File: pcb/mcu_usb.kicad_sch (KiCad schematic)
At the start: 33 parts, among them J12 USB_C_Receptacle, J13 UPDI, U10 CP2102N-A02-GQFN24, U11 LP2985-3.3, U9 AVR128DA32-I/PT, Y1 32.768kHz

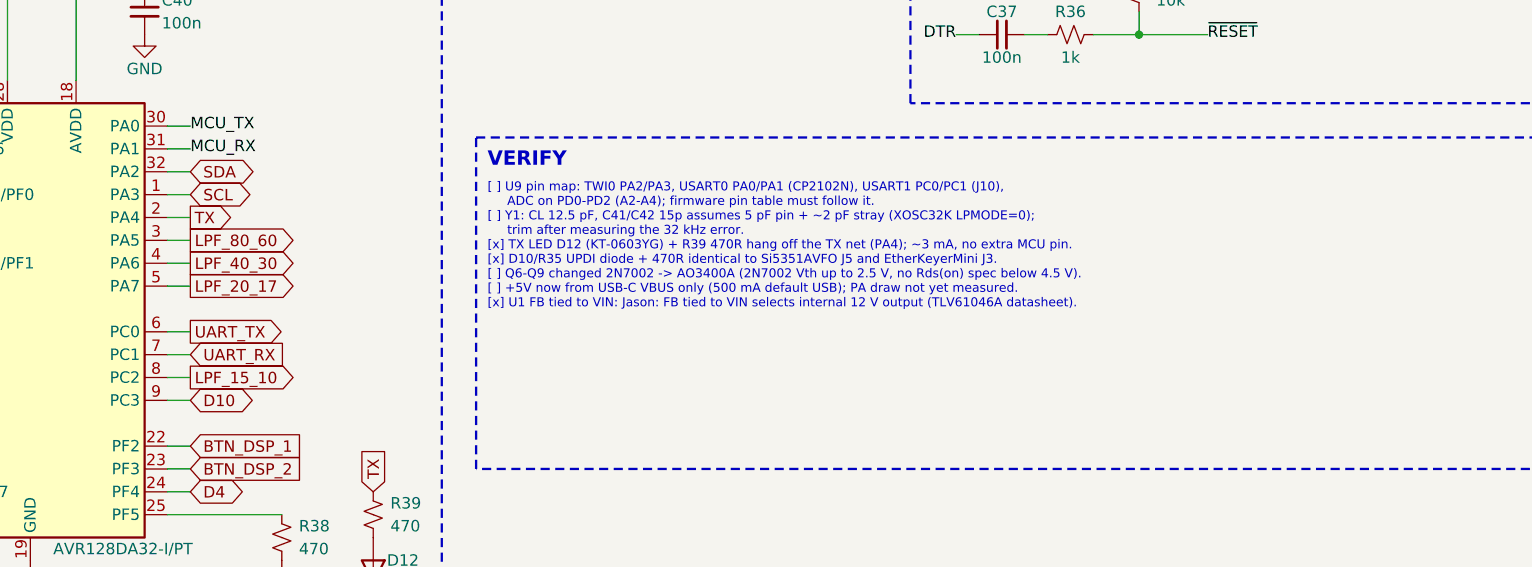
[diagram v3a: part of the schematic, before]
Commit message: Filter bank: 6-relay two-level tree driven by BAND_A/BAND_B
Replace the 8-relay, 4-driver bank with a 2-bit tree (K1-K3 input,
K4-K6 output, one G6K pole each). All relays off selects 80/60 m.
Q6/Q7 AO3400A drive the first and second levels; PA7/PC2 freed.
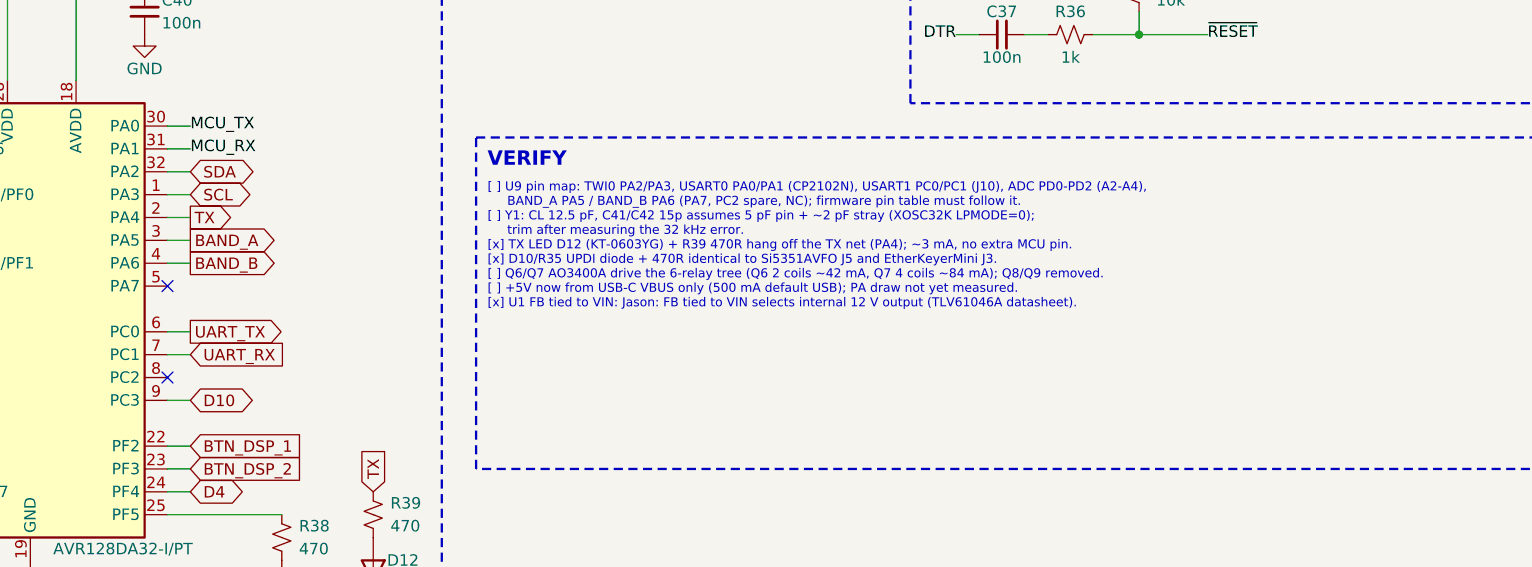
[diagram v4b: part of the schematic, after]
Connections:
- net LPF_15_10: no longer names the net of U9.8 (PC2)
- net LPF_20_17: no longer names the net of U9.5 (PA7)
- net LPF_40_30 renamed BAND_B
- net LPF_80_60 renamed BAND_A
- no-connect marks 15 -> 17
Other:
- note added: "[ ] U9 pin map: TWI0 PA2/PA3, USART0 PA0/PA1 (CP2102N), USART1 PC0/PC1 (J10), ADC PD0-PD2 (A2-A4), BAND_A PA5 / BAND_B PA6 (PA7, PC2 spare, NC); firmware pin table must follow it. [ ] Y1: CL 12.5 pF, C41/C42 15p assumes 5 pF pin + ~2 pF stray (XOSC32K LPMODE=0); trim after measuring the 32 kHz error. [x] TX LED D12 (KT-0603YG) + R39 470R hang off the TX net (PA4); ~3 mA, no extra MCU pin. [x] D10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"
- note removed: "[ ] U9 pin map: TWI0 PA2/PA3, USART0 PA0/PA1 (CP2102N), USART1 PC0/PC1 (J10), ADC on PD0-PD2 (A2-A4); firmware pin table must follow it. [ ] Y1: CL 12.5 pF, C41/C42 15p assumes 5 pF pin + ~2 pF stray (XOSC32K LPMODE=0); trim after measuring the 32 kHz error. [x] TX LED D12 (KT-0603YG) + R39 470R hang off the TX net (PA4); ~3 mA, no extra MCU pin. [x] D10/R35 UPDI diode + 470R identical to Si5351A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"
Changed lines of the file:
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@@
 		)
 	)
-	(global_label "LPF_80_60"
+	(global_label "BAND_A"
 		(shape output)
 		(at 119.38 139.7 0)
@@
 		)
 	)
-	(global_label "LPF_40_30"
+	(global_label "BAND_B"
 		(shape output)
 		(at 119.38 142.24 0)
@@
 		(property "Intersheetrefs" "${INTERSHEET_REFS}"
 			(at 119.38 142.24 0)
-			(effects
-				(font
-					(size 1.27 1.27)
-				)
-				(hide yes)
-			)
-		)
-	)
-	(wire
-		(pts
-			(xy 116.84 144.78)
-			(xy 119.38 144.78)
-		)
-		(stroke
-			(width 0)
-			(type default)
-		)
-	)
-	(global_label "LPF_20_17"
-		(shape output)
-		(at 119.38 144.78 0)
-		(fields_autoplaced yes)
-		(effects
-			(font
-				(size 1.27 1.27)
-				(color 0 120 120 1)
-			)
-			(justify left)
-		)
-		(property "Intersheetrefs" "${INTERSHEET_REFS}"
-			(at 119.38 144.78 0)
-			(effects
-				(font
-					(size 1.27 1.27)
-				)
-				(hide yes)
-			)
-		)
-	)
-	(wire
-		(pts
-			(xy 116.84 154.94)
-			(xy 119.38 154.94)
-		)
-		(stroke
-			(width 0)
-			(type default)
-		)
-	)
-	(global_label "LPF_15_10"
-		(shape output)
-		(at 119.38 154.94 0)
-		(fields_autoplaced yes)
-		(effects
-			(font
-				(size 1.27 1.27)
-				(color 0 120 120 1)
-			)
-			(justify left)
-		)
-		(property "Intersheetrefs" "${INTERSHEET_REFS}"
-			(at 119.38 154.94 0)
 			(effects
 				(font
@@
 			)
 		)
+	)
+	(no_connect
+		(at 116.84 144.78)
+	)
+	(no_connect
+		(at 116.84 154.94)
 	)
 	(wire
@@
 		)
 	)
-	(text "[ ] U9 pin map: TWI0 PA2/PA3, USART0 PA0/PA1 (CP2102N), USART1 PC0/PC1 (J10),\n     ADC on PD0-PD2 (A2-A4); firmware pin table must follow it.\n[ ] Y1: CL 12.5 pF, C41/C42 15p assumes 5 pF pin + ~2 pF stray (XOSC32K LPMODE=0);\n     trim after measuring the 32 kHz error.\n[x] TX LED D12 (KT-0603YG) + R39 470R hang off the TX net (PA4); ~3 mA, no extra MCU pin.\n[x] D10/R35 UPDI diode + 470R identical to Si5351AVFO J5 and EtherKeyerMini J3.\n[ ] Q6-Q9 changed 2N7002 -> AO3400A (2N7002 Vth up to 2.5 V, no Rds(on) spec below 4.5 V).\n[ ] +5V now from USB-C VBUS only (500 mA default USB); PA draw not yet measured.\n[x] U1 FB tied to VIN: Jason: FB tied to VIN selects internal 12 V output (TLV61046A datasheet)."
+	(text "[ ] U9 pin map: TWI0 PA2/PA3, USART0 PA0/PA1 (CP2102N), USART1 PC0/PC1 (J10), ADC PD0-PD2 (A2-A4),\n     BAND_A PA5 / BAND_B PA6 (PA7, PC2 spare, NC); firmware pin table must follow it.\n[ ] Y1: CL 12.5 pF, C41/C42 15p assumes 5 pF pin + ~2 pF stray (XOSC32K LPMODE=0);\n     trim after measuring the 32 kHz error.\n[x] TX LED D12 (KT-0603YG) + R39 470R hang off the TX net (PA4); ~3 mA, no extra MCU pin.\n[x] D10/R35 UPDI diode + 470R identical to Si5351AVFO J5 and EtherKeyerMini J3.\n[ ] Q6/Q7 AO3400A drive the 6-relay tree (Q6 2 coils ~42 mA, Q7 4 coils ~84 mA); Q8/Q9 removed.\n[ ] +5V now from USB-C VBUS only (500 mA default USB); PA draw not yet measured.\n[x] U1 FB tied to VIN: Jason: FB tied to VIN selects internal 12 V output (TLV61046A datasheet)."
 		(exclude_from_sim no)
 		(at 152.4 133.35 0)

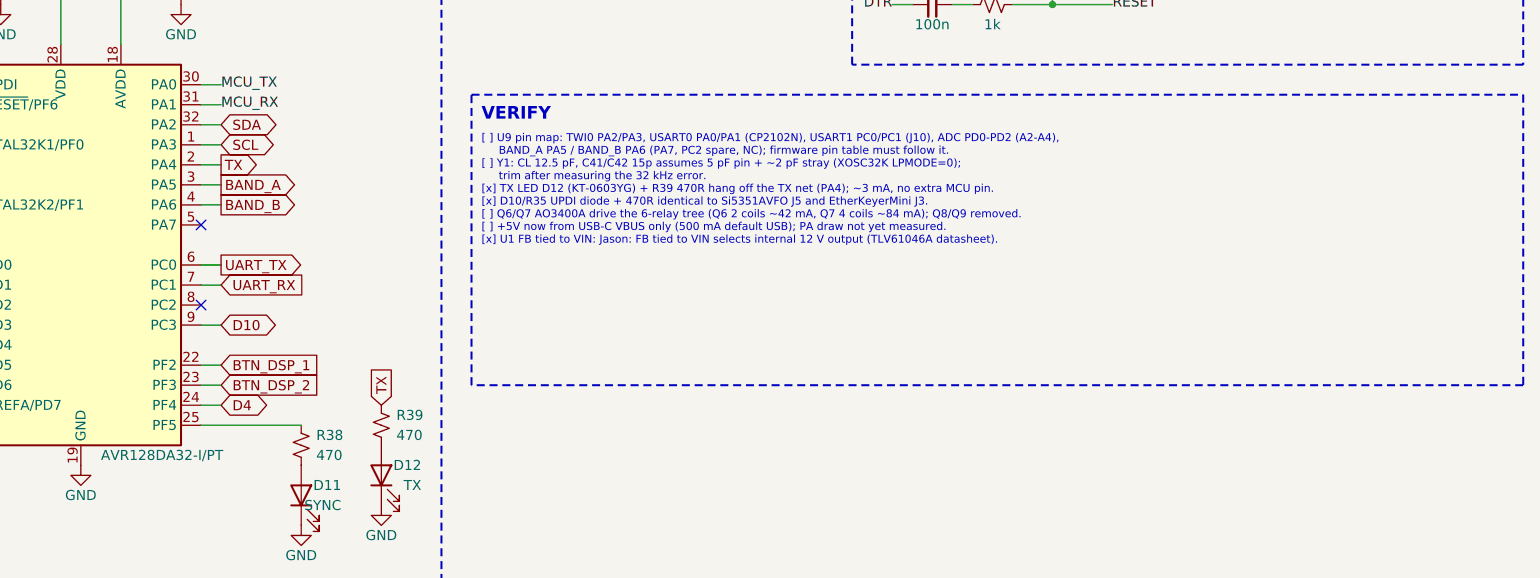
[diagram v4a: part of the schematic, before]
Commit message: Add GPS option sheet (u-blox MAX-M10S) on USART2 ALT1
- New pcb/gps.kicad_sch: MAX-M10S U12 on +3.3V (VIO_SEL open), UART to
  PF4/PF5, TIMEPULSE via 470R to GPS_PPS / J14, active-antenna bias-T
  (10R, 10n, 27nH per IM 4.3.4) to U.FL J15, supercap V_BCKP via
  1N5711W + 1k.
- MCU: D4 moved PF4 -> PA7, sync LED moved PF5 -> PC2.
- GPS_PPS MCU pin left open; options in VERIFY.md.
- Regenerated schematic PDF; ERC 0 errors.
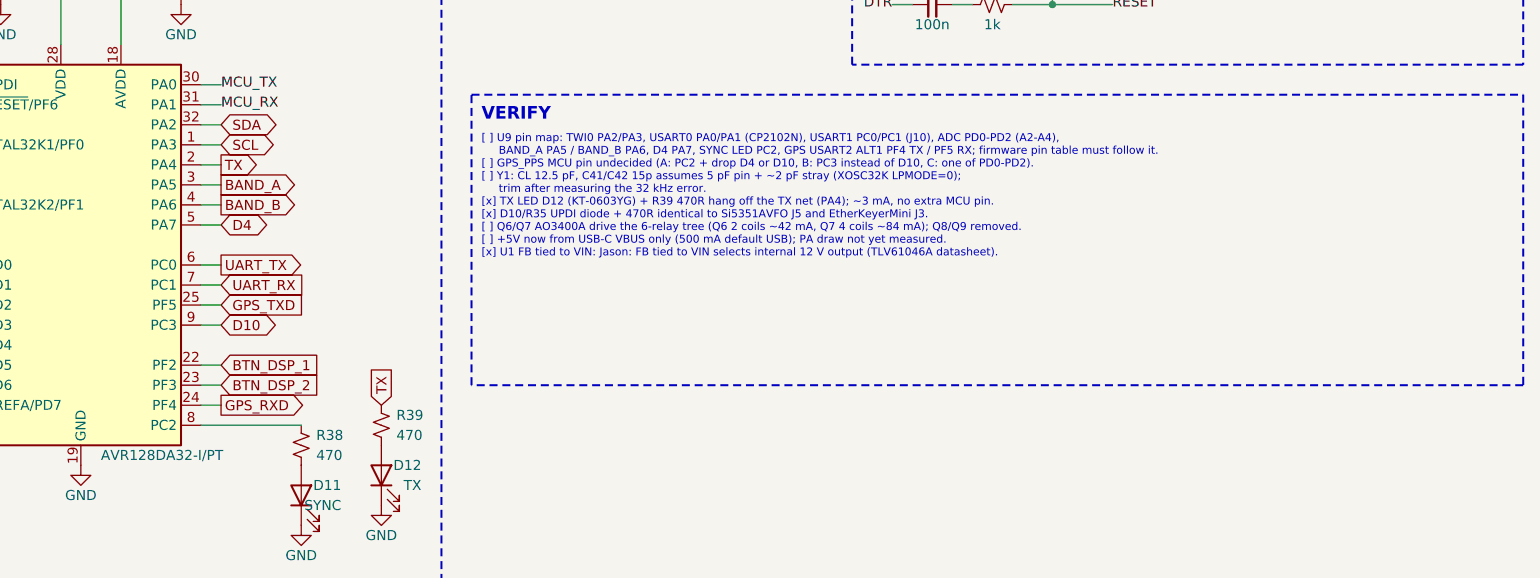
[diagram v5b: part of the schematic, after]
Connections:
- net D4: now also U9.5 (PA7); no longer U9.24 (PF4)
- net at R38.1: now also U9.8 (PC2); no longer U9.25 (PF5)
- new net GPS_RXD: U9.24 (PF4)
- new net GPS_TXD: U9.25 (PF5)
- no-connect marks 17 -> 15
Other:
- note added: "[ ] U9 pin map: TWI0 PA2/PA3, USART0 PA0/PA1 (CP2102N), USART1 PC0/PC1 (J10), ADC PD0-PD2 (A2-A4), BAND_A PA5 / BAND_B PA6, D4 PA7, SYNC LED PC2, GPS USART2 ALT1 PF4 TX / PF5 RX; firmware pin table must follow it. [ ] GPS_PPS MCU pin undecided (A: PC2 + drop D4 or D10, B: PC3 instead of D10, C: one of PD0-PD2). [ ] Y1: CL 12.5 pF, C41/C42 15p assumes 5 pF pin + ~2 pF stray (XOSC32K LPMODE=0); tri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"
- note removed: "[ ] U9 pin map: TWI0 PA2/PA3, USART0 PA0/PA1 (CP2102N), USART1 PC0/PC1 (J10), ADC PD0-PD2 (A2-A4), BAND_A PA5 / BAND_B PA6 (PA7, PC2 spare, NC); firmware pin table must follow it. [ ] Y1: CL 12.5 pF, C41/C42 15p assumes 5 pF pin + ~2 pF stray (XOSC32K LPMODE=0); trim after measuring the 32 kHz error. [x] TX LED D12 (KT-0603YG) + R39 470R hang off the TX net (PA4); ~3 mA, no extra MCU pin. [x] D10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"
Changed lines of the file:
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@@
 		(pin "7"
 		)
+		(pin "25"
+		)
+		(pin "9"
+		)
+		(pin "22"
+		)
+		(pin "23"
+		)
+		(pin "24"
+		)
 		(pin "8"
-		)
-		(pin "9"
-		)
-		(pin "22"
-		)
-		(pin "23"
-		)
-		(pin "24"
-		)
-		(pin "25"
 		)
 		(pin "27"
@@
 	(wire
 		(pts
+			(xy 116.84 144.78)
+			(xy 119.38 144.78)
+		)
+		(stroke
+			(width 0)
+			(type default)
+		)
+	)
+	(global_label "D4"
+		(shape bidirectional)
+		(at 119.38 144.78 0)
+		(fields_autoplaced yes)
+		(effects
+			(font
+				(size 1.27 1.27)
+				(color 0 0 0 1)
+			)
+			(justify left)
+		)
+		(property "Intersheetrefs" "${INTERSHEET_REFS}"
+			(at 119.38 144.78 0)
+			(effects
+				(font
+					(size 1.27 1.27)
+				)
+				(hide yes)
+			)
+		)
+	)
+	(wire
+		(pts
 			(xy 116.84 167.64)
 			(xy 119.38 167.64)
@@
 		)
 	)
-	(global_label "D4"
-		(shape bidirectional)
+	(global_label "GPS_RXD"
+		(shape output)
 		(at 119.38 167.64 0)
 		(fields_autoplaced yes)
@@
 			(font
 				(size 1.27 1.27)
-				(color 0 0 0 1)
+				(color 0 0 200 1)
 			)
 			(justify left)
@@
 		(property "Intersheetrefs" "${INTERSHEET_REFS}"
 			(at 119.38 167.64 0)
+			(effects
+				(font
+					(size 1.27 1.27)
+				)
+				(hide yes)
+			)
+		)
+	)
+	(wire
+		(pts
+			(xy 116.84 154.94)
+			(xy 119.38 154.94)
+		)
+		(stroke
+			(width 0)
+			(type default)
+		)
+	)
+	(global_label "GPS_TXD"
+		(shape input)
+		(at 119.38 154.94 0)
+		(fields_autoplaced yes)
+		(effects
+			(font
+				(size 1.27 1.27)
+				(color 0 0 200 1)
+			)
+			(justify left)
+		)
+		(property "Intersheetrefs" "${INTERSHEET_REFS}"
+			(at 119.38 154.94 0)
 			(effects
 				(font
@@
 			)
 		)
-	)
-	(no_connect
-		(at 116.84 144.78)
-	)
-	(no_connect
-		(at 116.84 154.94)
 	)
 	(wire
@@
 		)
 	)
-	(text "[ ] U9 pin map: TWI0 PA2/PA3, USART0 PA0/PA1 (CP2102N), USART1 PC0/PC1 (J10), ADC PD0-PD2 (A2-A4),\n     BAND_A PA5 / BAND_B PA6 (PA7, PC2 spare, NC); firmware pin table must follow it.\n[ ] Y1: CL 12.5 pF, C41/C42 15p assumes 5 pF pin + ~2 pF stray (XOSC32K LPMODE=0);\n     trim after measuring the 32 kHz error.\n[x] TX LED D12 (KT-0603YG) + R39 470R hang off the TX net (PA4); ~3 mA, no extra MCU pin.\n[x] D10/R35 UPDI diode + 470R identical to Si5351AVFO J5 and EtherKeyerMini J3.\n[ ] Q6/Q7 AO3400A drive the 6-relay tree (Q6 2 coils ~42 mA, Q7 4 coils ~84 mA); Q8/Q9 removed.\n[ ] +5V now from USB-C VBUS only (500 mA default USB); PA draw not yet measured.\n[x] U1 FB tied to VIN: Jason: FB tied to VIN selects internal 12 V output (TLV61046A datasheet)."
+	(text "[ ] U9 pin map: TWI0 PA2/PA3, USART0 PA0/PA1 (CP2102N), USART1 PC0/PC1 (J10), ADC PD0-PD2 (A2-A4),\n     BAND_A PA5 / BAND_B PA6, D4 PA7, SYNC LED PC2, GPS USART2 ALT1 PF4 TX / PF5 RX; firmware pin table must follow it.\n[ ] GPS_PPS MCU pin undecided (A: PC2 + drop D4 or D10, B: PC3 instead of D10, C: one of PD0-PD2).\n[ ] Y1: CL 12.5 pF, C41/C42 15p assumes 5 pF pin + ~2 pF stray (XOSC32K LPMODE=0);\n     trim after measuring the 32 kHz error.\n[x] TX LED D12 (KT-0603YG) + R39 470R hang off the TX net (PA4); ~3 mA, no extra MCU pin.\n[x] D10/R35 UPDI diode + 470R identical to Si5351AVFO J5 and EtherKeyerMini J3.\n[ ] Q6/Q7 AO3400A drive the 6-relay tree (Q6 2 coils ~42 mA, Q7 4 coils ~84 mA); Q8/Q9 removed.\n[ ] +5V now from USB-C VBUS only (500 mA default USB); PA draw not yet measured.\n[x] U1 FB tied to VIN: Jason: FB tied to VIN selects internal 12 V output (TLV61046A datasheet)."
 		(exclude_from_sim no)
 		(at 152.4 133.35 0)
